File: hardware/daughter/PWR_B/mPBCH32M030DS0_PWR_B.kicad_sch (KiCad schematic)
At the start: 0 parts

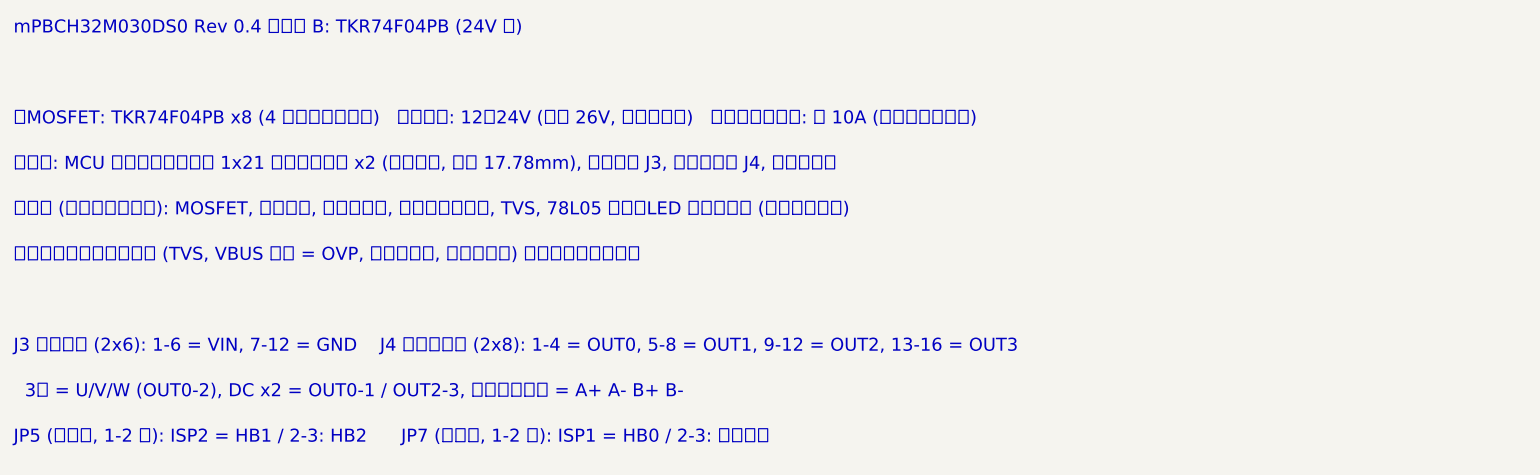
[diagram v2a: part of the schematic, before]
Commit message: 子基板 B を 44.6 x 99.5mm に拡大: M3 丸端子台 x6・ヒートシンク固定穴 x2・電源ベタのはんだ盛り
- 電源 (J3 VIN / J5 GND) と 4 相出力 (J40〜J43) を Würth REDCUBE の M3 丸端子台で受ける
- ヒートシンク固定用 M3 穴 H1/H2。MOSFET・シャントは BOTTOM 面 (ヒートシンク側) に 4 レッグ横並び
- 大電流の銅箔を配線前に固定ベタとして置き, レジスト開口ではんだを盛れるようにした
- 右端の VBUS 帯を表裏 2 層に, レッグ 3 横のネックを裏で迂回, 上端に USB 帰路の GND 帯
- 電流容量 (1 相): 1oz 5.4A / はんだ 0.3mm 7.4A。USB-PD 経路は 3A まで
- D1/C1 の − 側は ISH。面付けパネル (99.94 x 99.76mm), 製造データ, 資料を更新

Co-Authored-By: Claude Opus 5.5 <noreply@anthropic.com>
Claude-Session: https://claude.ai/code/session_01LENFjjhDfYjJZV1NWhB9uV
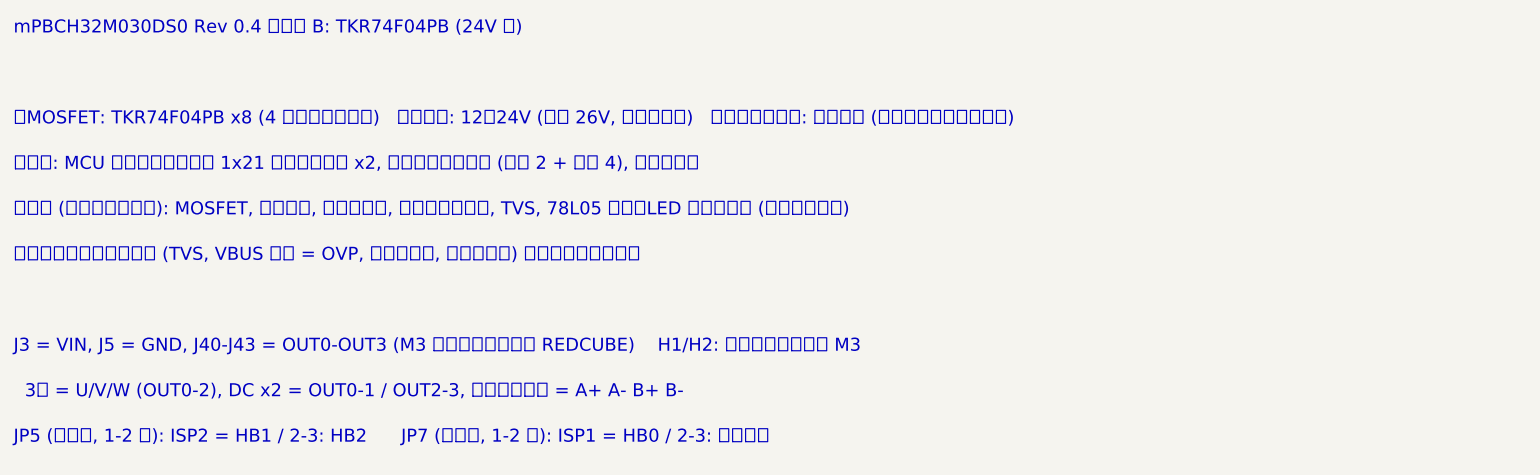
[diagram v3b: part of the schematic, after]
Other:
- note added: "J3 = VIN, J5 = GND, J40-J43 = OUT0-OUT3 (M3 丸端子用ネジ端子 REDCUBE) H1/H2: ヒートシンク固定 M3"
- note added: "・MOSFET: TKR74F04PB x8 (4 ハーフブリッジ) 入力電圧: 12〜24V (上限 26V, 安定化電源) 出力電流の目安: 銅箔律速 (電流容量チェック参照)"
- note added: "・上面: MCU モジュールを挿す 1x21 ピンソケット x2, 丸端子用ネジ端子 (電源 2 + 出力 4), バルク容量"
- note removed: "J3 電源入力 (2x6): 1-6 = VIN, 7-12 = GND J4 モータ出力 (2x8): 1-4 = OUT0, 5-8 = OUT1, 9-12 = OUT2, 13-16 = OUT3"
- note removed: "・MOSFET: TKR74F04PB x8 (4 ハーフブリッジ) 入力電圧: 12〜24V (上限 26V, 安定化電源) 出力電流の目安: 約 10A (ピンヘッダ律速)"
- note removed: "・上面: MCU モジュールを挿す 1x21 ピンソケット x2 (左右対称, 列間 17.78mm), 電源入力 J3, モータ出力 J4, バルク容量"
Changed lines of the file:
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@@
 (text "mPBCH32M030DS0 Rev 0.4 子基板 B: TKR74F04PB (24V 系)" (exclude_from_sim no) (at 20 30 0) (effects (font (size 2 2)) (justify left bottom)))
 (text "" (exclude_from_sim no) (at 20 37 0) (effects (font (size 2 2)) (justify left bottom)))
-(text "・MOSFET: TKR74F04PB x8 (4 ハーフブリッジ)   入力電圧: 12〜24V (上限 26V, 安定化電源)   出力電流の目安: 約 10A (ピンヘッダ律速)" (exclude_from_sim no) (at 20 44 0) (effects (font (size 2 2)) (justify left bottom)))
-(text "・上面: MCU モジュールを挿す 1x21 ピンソケット x2 (左右対称, 列間 17.78mm), 電源入力 J3, モータ出力 J4, バルク容量" (exclude_from_sim no) (at 20 51 0) (effects (font (size 2 2)) (justify left bottom)))
+(text "・MOSFET: TKR74F04PB x8 (4 ハーフブリッジ)   入力電圧: 12〜24V (上限 26V, 安定化電源)   出力電流の目安: 銅箔律速 (電流容量チェック参照)" (exclude_from_sim no) (at 20 44 0) (effects (font (size 2 2)) (justify left bottom)))
+(text "・上面: MCU モジュールを挿す 1x21 ピンソケット x2, 丸端子用ネジ端子 (電源 2 + 出力 4), バルク容量" (exclude_from_sim no) (at 20 51 0) (effects (font (size 2 2)) (justify left bottom)))
 (text "・下面 (ヒートシンク側): MOSFET, シャント, ゲート抵抗, 理想ダイオード, TVS, 78L05 など。LED は置かない (モジュール側)" (exclude_from_sim no) (at 20 58 0) (effects (font (size 2 2)) (justify left bottom)))
 (text "・電圧系に依存する部品 (TVS, VBUS 分圧 = OVP, バルク容量, 相電圧分圧) はこの基板で決める" (exclude_from_sim no) (at 20 65 0) (effects (font (size 2 2)) (justify left bottom)))
 (text "" (exclude_from_sim no) (at 20 72 0) (effects (font (size 2 2)) (justify left bottom)))
-(text "J3 電源入力 (2x6): 1-6 = VIN, 7-12 = GND    J4 モータ出力 (2x8): 1-4 = OUT0, 5-8 = OUT1, 9-12 = OUT2, 13-16 = OUT3" (exclude_from_sim no) (at 20 79 0) (effects (font (size 2 2)) (justify left bottom)))
+(text "J3 = VIN, J5 = GND, J40-J43 = OUT0-OUT3 (M3 丸端子用ネジ端子 REDCUBE)    H1/H2: ヒートシンク固定 M3" (exclude_from_sim no) (at 20 79 0) (effects (font (size 2 2)) (justify left bottom)))
 (text "  3相 = U/V/W (OUT0-2), DC x2 = OUT0-1 / OUT2-3, ステッピング = A+ A- B+ B-" (exclude_from_sim no) (at 20 86 0) (effects (font (size 2 2)) (justify left bottom)))
 (text "JP5 (はんだ, 1-2 済): ISP2 = HB1 / 2-3: HB2      JP7 (はんだ, 1-2 済): ISP1 = HB0 / 2-3: バス電流" (exclude_from_sim no) (at 20 93 0) (effects (font (size 2 2)) (justify left bottom)))
